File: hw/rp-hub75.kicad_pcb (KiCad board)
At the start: 2 copper layers, 45 x 45 mm, 38 parts, among them J1 Display Connector, J2 USB_C_Receptacle_USB2.0_16P, J3 Screw_Terminal_01x02, J4 Conn_01x04, J5 USB_A, J6 Conn_01x10, U1 AMS1117-3.3, U2 RP2350_60QFN, U3 W25Q128JVS, Y1 TXM12M0004322CBCDO00T

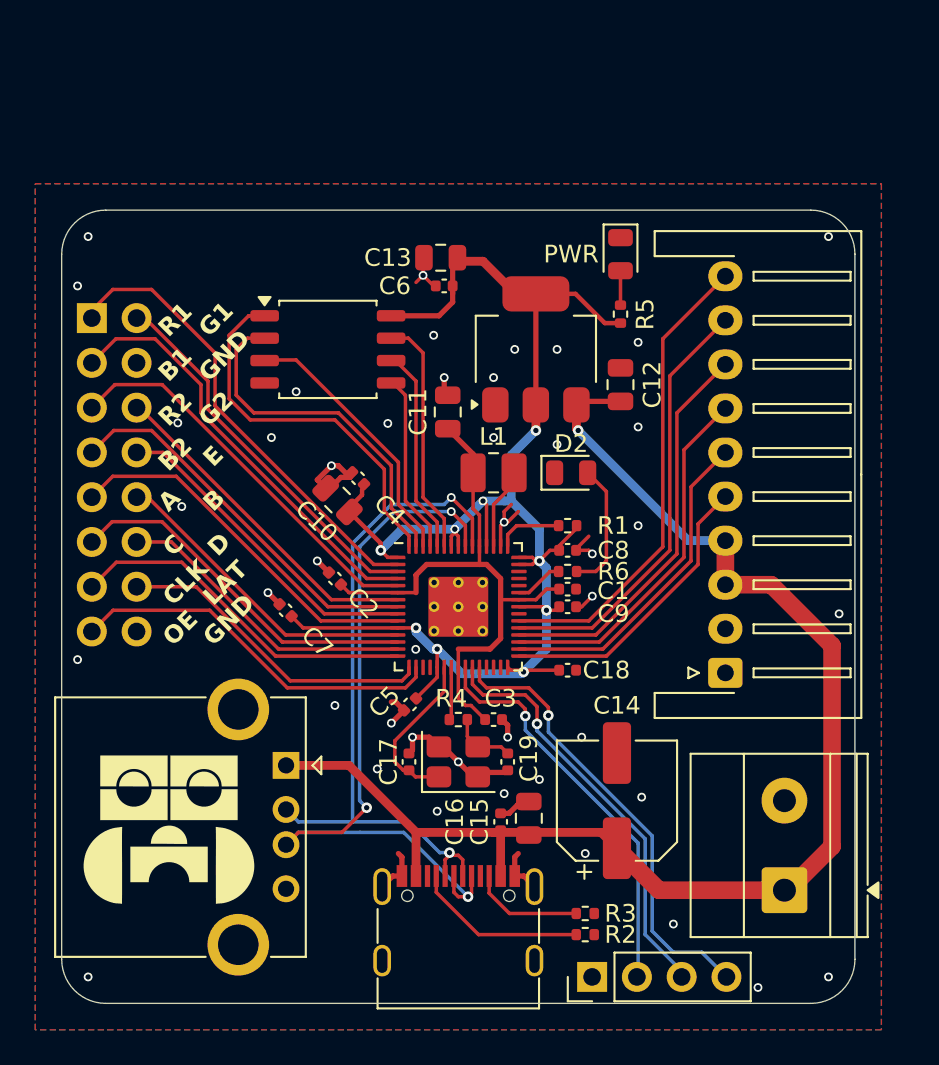
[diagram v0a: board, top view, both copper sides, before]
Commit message: hw: edit DBG connector, new capacitor
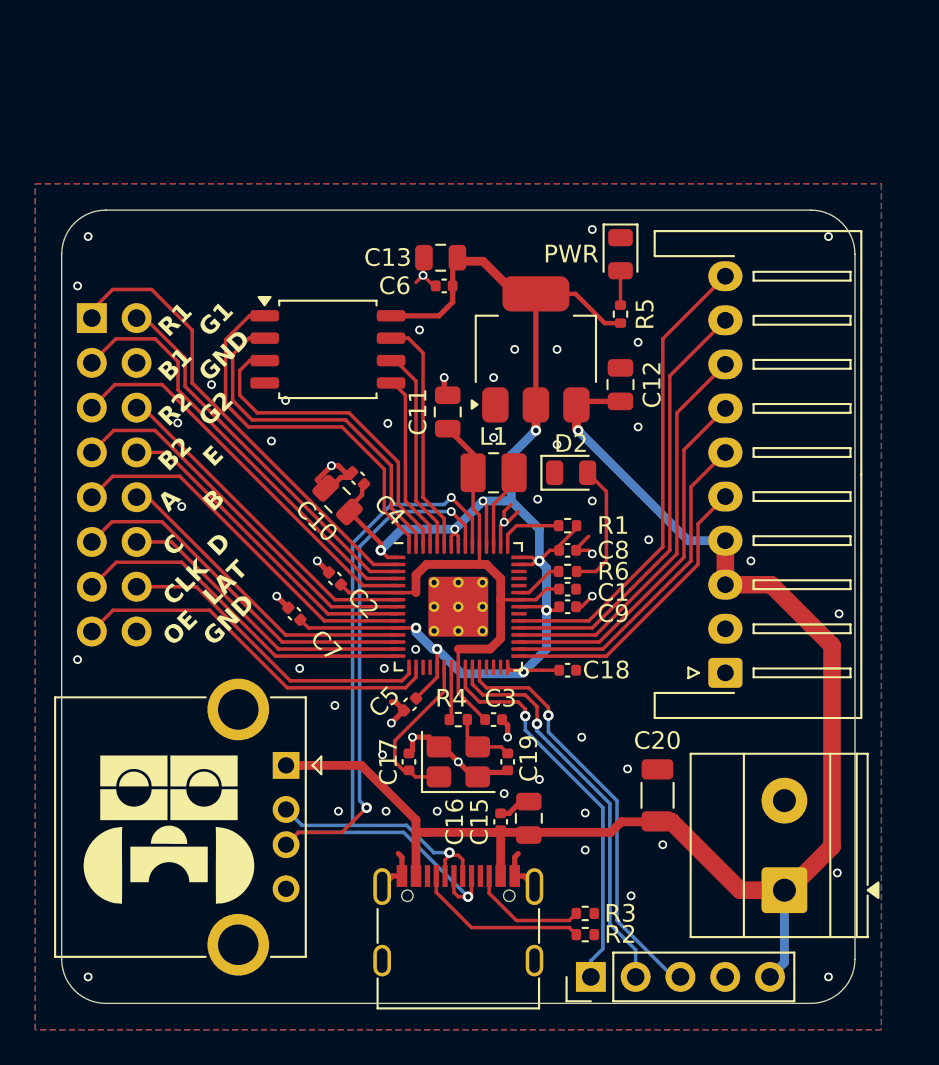
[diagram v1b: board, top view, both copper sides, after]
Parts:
- removed C14: 470u, Capacitor_SMD:CP_Elec_6.3x7.7
- removed J4: Conn_01x04, Connector_PinHeader_2.54mm:PinHeader_1x04_P2.54mm_Vertical
- added C20: 47u, Capacitor_SMD:C_1206_3216Metric, F.Cu at (211.3, 110.7)
- added J7: Conn_01x05, Connector_PinHeader_2.54mm:PinHeader_1x05_P2.54mm_Vertical, F.Cu at (207.5, 121.0)
- moved C7 0.54 mm to (190.7, 100.4)
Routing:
- net +5V: track 77.2 -> 83.4 mm
- net /QSPI_SD2: track 15.3 -> 19.0 mm
- net Net-(J7-Pin_3): track 25.7 -> 24.3 mm
- net Net-(J7-Pin_2): track 23.9 -> 22.8 mm
- net +3V3: track 87.4 -> 86.9 mm
- net Net-(J7-Pin_1): track 22.9 -> 22.4 mm
- net GND: vias 44 -> 55
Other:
- board text added: "10/2025"
- board text added: "V1.1"
- board text removed: "9/2025"
- board text removed: "V1"

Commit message: V1.2
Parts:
- added J4: Conn_01x02, Connector_PinHeader_2.54mm:PinHeader_1x02_P2.54mm_Vertical, F.Cu at (180.3, 79.4)
- added REF**: MountingHole_3.2mm_M3, MountingHole:MountingHole_3.2mm_M3, F.Cu at (181.0, 74.0)
- added REF**: MountingHole_3.2mm_M3, MountingHole:MountingHole_3.2mm_M3, F.Cu at (219.0, 106.5)
- R5, R6: value 220 -> 1k
- U3: value W25Q128JVS -> ZD25WQ80CTIGT; footprint Package_SO:SOIC-8_5.3x5.3mm_P1.27mm -> Package_SO:SOIC-8_3.9x4.9mm_P1.27mm
- moved J6 26.9 mm to (210.2, 77.3), turned to 180 degrees
- moved R3 14.2 mm to (193.1, 118.7), turned to 180 degrees
- moved R2 14.1 mm to (193.1, 117.5), turned to 180 degrees
- moved D2 13.7 mm to (209.3, 105.8)
- moved C12 8.44 mm to (211.0, 95.7), turned to -90 degrees
- moved C13 7.70 mm to (203.7, 86.3), turned to -90 degrees
- moved U1 5.46 mm to (208.5, 89.0)
- moved C6 4.82 mm to (202.0, 85.7), turned to -90 degrees
- moved D1 4.08 mm to (206.8, 83.3), turned to 0 degrees
- moved J3 3.27 mm to (219.9, 119.0)
- moved C11 2.58 mm to (201.9, 89.6), turned to 0 degrees
- moved U3 2.47 mm to (195.0, 86.0)
- moved J7 2.14 mm to (209.6, 120.5), turned to 180 degrees
- moved C20 1.68 mm to (212.9, 110.2), turned to -90 degrees
- moved J1 1.10 mm to (180.3, 83.6)
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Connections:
- J3 pad 1: +5V -> GND
- J3 pad 2: GND -> +5V
- J7 pad 1: Net-(J7-Pin_1) -> GND
- J7 pad 2: Net-(J7-Pin_2) -> +5V
- J7 pad 4: GND -> Net-(J7-Pin_4)
- J7 pad 5: +5V -> Net-(J7-Pin_5)
- U2 pad 24: Net-(J7-Pin_1) -> Net-(J7-Pin_3)
- U2 pad 25: Net-(J7-Pin_2) -> Net-(J7-Pin_4)
- U2 pad 26: Net-(J7-Pin_3) -> Net-(J7-Pin_5)
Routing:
- net Net-(J7-Pin_2): track 22.8 -> 0.00 mm, vias 1 -> 0
- net Net-(J7-Pin_1): track 22.4 -> 0.00 mm, vias 1 -> 0
- net SPI_MISO: track 16.8 -> 37.2 mm, vias 0 -> 1
- net GND: track 34.9 -> 16.2 mm, vias 55 -> 52
- net SPI_MOSI: track 18.8 -> 37.1 mm, vias 0 -> 1
- net SPI_CS: track 20.8 -> 37.0 mm, vias 0 -> 1
- net SPI_SCK: track 22.8 -> 38.1 mm, vias 0 -> 1
- net Net-(J7-Pin_4): track 0.00 -> 14.5 mm
- net SPI_X1: track 24.7 -> 39.2 mm, vias 0 -> 1
- net SPI_X2: track 26.7 -> 40.2 mm, vias 0 -> 1
- net Net-(J7-Pin_5): track 0.00 -> 11.8 mm
- net +5V: track 83.4 -> 94.4 mm, vias 1 -> 0
- net Net-(J7-Pin_3): track 24.3 -> 17.2 mm, vias 1 -> 0
- net /QSPI_SS: track 21.9 -> 28.4 mm
- net Net-(D2-A): track 7.38 -> 11.8 mm
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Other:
- board size 45 x 45 mm -> 45 x 52 mm
- board text added: "12/2025"
- board text added: "DBG"
- board text added: "V1.2"
- board text removed: "10/2025"
- board text removed: "V1.1"

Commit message: V1.3
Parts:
- added J8: Conn_01x04, Connector_PinHeader_2.54mm:PinHeader_1x04_P2.54mm_Vertical, F.Cu at (183.2, 104.7)
- moved D1 23.0 mm to (208.5, 106.2), turned to 90 degrees
- moved R5 22.1 mm to (206.2, 105.3), turned to 0 degrees
- moved R2 14.0 mm to (206.8, 120.4), turned to 0 degrees
- moved R3 13.7 mm to (206.8, 119.2), turned to 0 degrees
- moved J5 6.77 mm to (183.5, 109.8), turned to 0 degrees
- moved J6 2.00 mm to (210.2, 75.3)
- moved D2 1.46 mm to (210.7, 106.2), turned to 90 degrees
- moved C7 1.30 mm to (192.4, 100.5)
- moved U3 1.16 mm to (195.3, 87.1)
- moved C10 1.03 mm to (195.6, 93.1)
- moved C11 1.03 mm to (194.2, 94.1)
- moved C2 0.90 mm to (193.9, 98.4)
- moved C15 0.64 mm to (204.5, 111.6)
- moved C16 0.58 mm to (202.9, 111.9)
- renumbered C4 to C10, C10 to C11, C6 to C17, C17 to C18, C11 to C4, C18 to C6
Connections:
- J6 pad 2: GND -> +5V
- J6 pad 4: +5V -> SPI_MISO
- J6 pad 5: SPI_MISO -> SPI_MOSI
- J6 pad 6: SPI_MOSI -> SPI_CS
- J6 pad 7: SPI_CS -> SPI_SCK
- J6 pad 8: SPI_SCK -> GND
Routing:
- net +5V: track 94.4 -> 106.6 mm
- net D-: track 39.4 -> 45.7 mm
- net Net-(J2-CC1): track 7.23 -> 10.8 mm
- net Net-(J2-CC2): track 10.4 -> 6.98 mm
- net +3V3: track 84.4 -> 81.2 mm
- net SPI_X1: track 39.2 -> 41.2 mm
- net SPI_X2: track 40.2 -> 42.2 mm
- net /QSPI_SCLK: track 12.1 -> 10.5 mm
- net Net-(D2-A): track 11.8 -> 10.4 mm
- net /QSPI_SD0: track 9.01 -> 7.79 mm
- net D+: track 44.0 -> 45.2 mm
- net SPI_MOSI: track 37.1 -> 38.1 mm
- net SPI_CS: track 37.0 -> 38.0 mm
- net SPI_MISO: track 37.2 -> 38.2 mm
- net +1V1: track 32.8 -> 31.9 mm
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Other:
- board text added: "3V3 LDO"
- board text added: "BOOT"
- board text added: "D+"
- board text added: "D-"
- board text added: "Flash"
- board text added: "RP2350"
- board text added: "RP2350 HUB75E"
- board text added: "V1.3"
- board text added: "display driver"
- board text removed: "RP2350 HUB75E driver"
- board text removed: "V1.2"

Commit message: V1.4
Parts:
- removed J4: Conn_01x02, Connector_PinHeader_2.54mm:PinHeader_1x02_P2.54mm_Vertical
- added SW1: SW_Push, Button_Switch_SMD:SW_SPST_TS-1088-xR025, F.Cu at (181.6, 79.3)
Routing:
- net GND: track 16.4 -> 15.0 mm, vias 72 -> 71
- net SPI_MISO: track 38.2 -> 39.4 mm
- net SPI_X2: track 42.2 -> 41.1 mm
- net /QSPI_SS: track 28.6 -> 27.5 mm
- net +5V: track 106.6 -> 105.9 mm
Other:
- board text added: "V1.4"
- board text removed: "V1.3"

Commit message: V1.4b
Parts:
- removed C20: 47u, Capacitor_SMD:C_1206_3216Metric
- moved J6 1.00 mm to (210.2, 76.3)
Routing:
- net +5V: track 105.9 -> 103.8 mm
- net SPI_X1: track 41.2 -> 40.2 mm
- net SPI_SCK: track 37.9 -> 36.9 mm
- net SPI_MOSI: track 38.0 -> 37.0 mm
- net SPI_MISO: track 39.4 -> 38.4 mm
- net SPI_CS: track 38.0 -> 37.0 mm
- net SPI_X2: track 41.1 -> 40.1 mm
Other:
- board text added: "1/2026"
- board text removed: "12/2025"

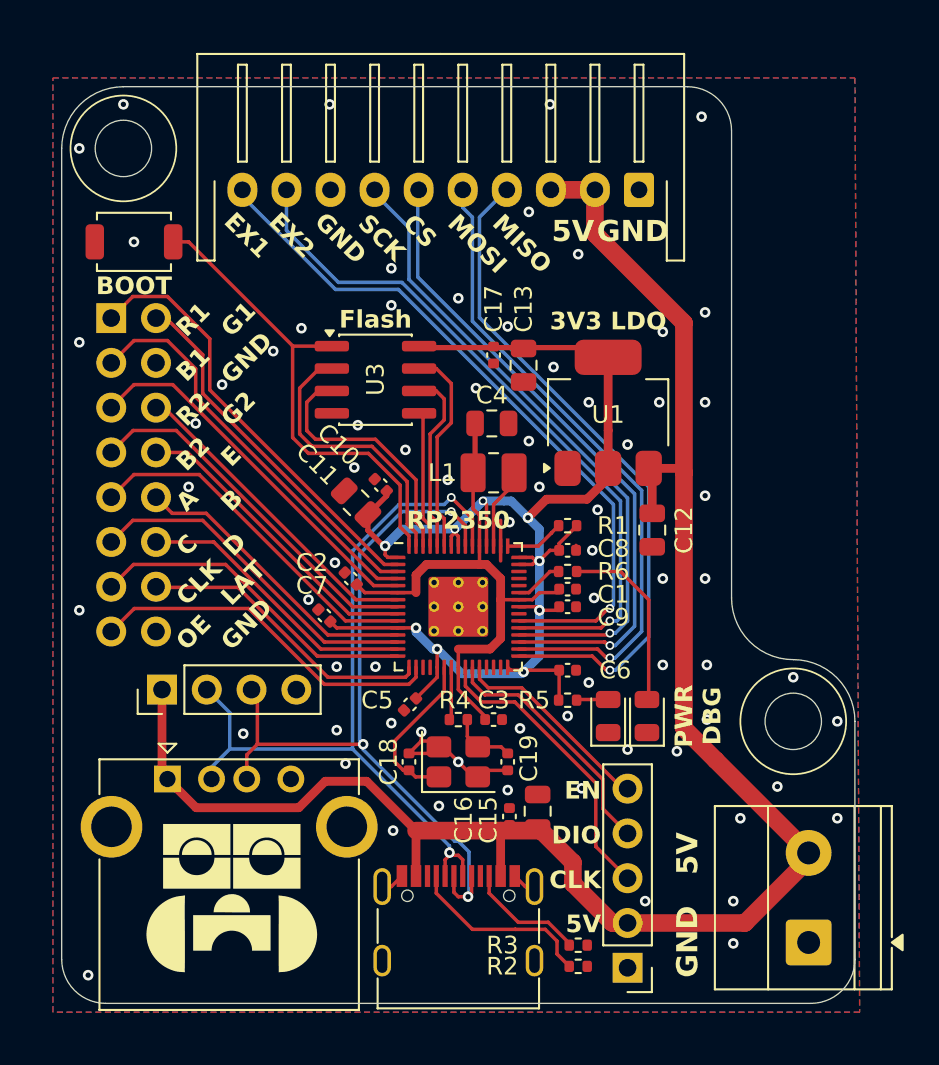
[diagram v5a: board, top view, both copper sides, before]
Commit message: v1.5 - use QSPI, better 1V1 line
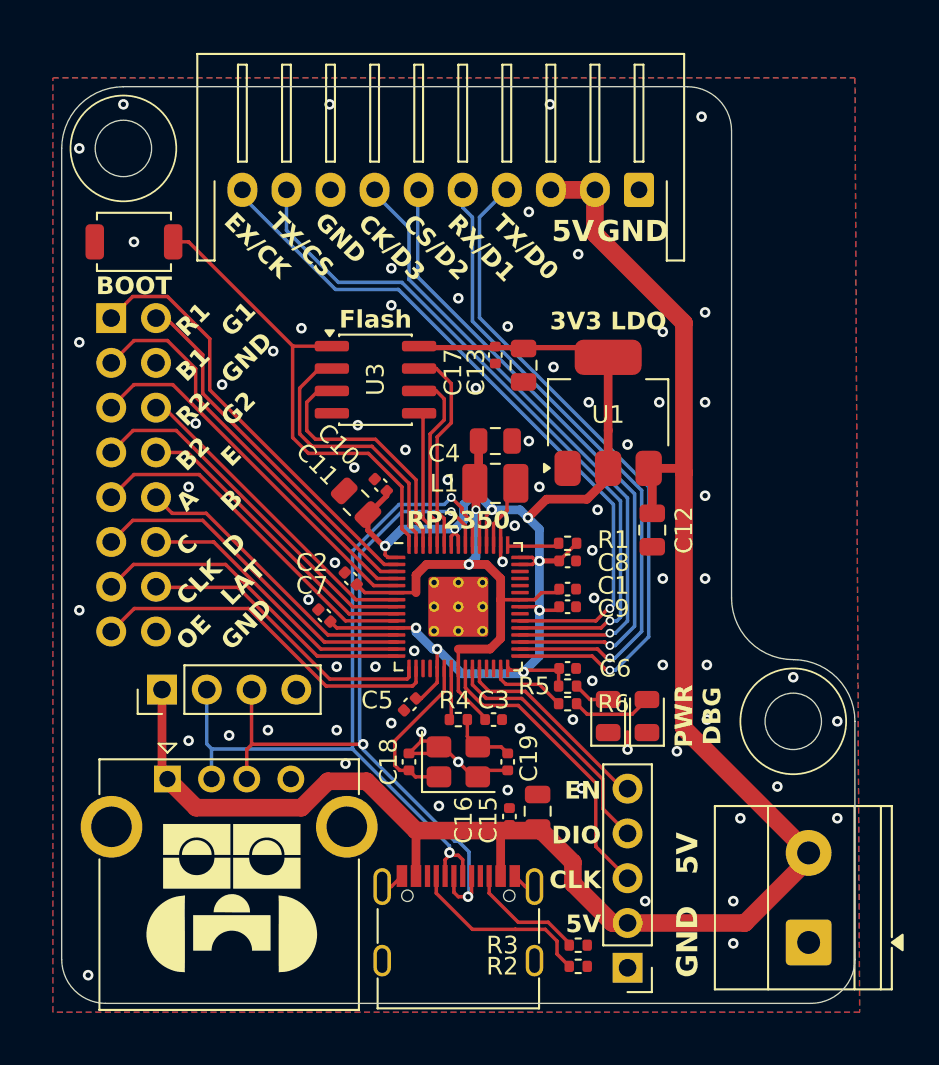
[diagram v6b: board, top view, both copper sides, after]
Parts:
- moved R6 7.50 mm to (206.2, 105.5)
- moved C4 1.02 mm to (202.1, 90.6)
- moved R1 1.00 mm to (206.2, 96.4)
- moved R5 0.80 mm to (206.2, 104.5)
- moved L1 0.61 mm to (202.1, 93.0)
- moved C8 0.60 mm to (206.2, 97.4)
- moved C17 0.10 mm to (202.1, 85.7)
- moved C6 0.10 mm to (206.2, 103.5)
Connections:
- net SPI_CS renamed SPI_CS/D2
- net SPI_MISO renamed SPI_TX/D0
- net SPI_MOSI renamed SPI_RX/D1
- net SPI_SCK renamed SPI_CK/D3
- net SPI_X1 renamed SPI_TX/CS
- net SPI_X2 renamed SPI_EX/CK
- U2 pad 29: unconnected-(U2-GPIO18-Pad29) -> STATUS
- U2 pad 40: STATUS -> unconnected-(U2-GPIO26_ADC0-Pad40)
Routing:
- net Net-(D2-A): track 10.4 -> 4.59 mm
- net STATUS: track 2.75 -> 4.53 mm
- net +1V1: track 31.9 -> 33.0 mm, vias 0 -> 2
- net +3V3: track 81.2 -> 80.3 mm
- net GND: track 15.0 -> 15.1 mm, vias 71 -> 74
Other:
- board text added: "2/2026"
- board text added: "CK/D3"
- board text added: "CS/D2"
- board text added: "EX/CK"
- board text added: "RX/D1"
- board text added: "TX/CS"
- board text added: "TX/D0"
- board text added: "V1.5"
- board text removed: "1/2026"
- board text removed: "CS"
- board text removed: "EX1"
- board text removed: "EX2"
- board text removed: "MISO"
- board text removed: "MOSI"
- board text removed: "SCK"
- board text removed: "V1.4"

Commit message: v1.6
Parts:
- removed J8: Conn_01x04, Connector_PinHeader_2.54mm:PinHeader_1x04_P2.54mm_Vertical
- added J4: Conn_01x03, Connector_PinHeader_2.54mm:PinHeader_1x03_P2.54mm_Vertical, F.Cu at (183.5, 106.0)
- moved C13 10.7 mm to (208.8, 95.7)
- moved C17 1.70 mm to (203.8, 85.8)
- moved C5 1.01 mm to (196.6, 106.3)
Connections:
- U2 pad 18: unconnected-(U2-GPIO14-Pad18) -> SDA
- U2 pad 19: unconnected-(U2-GPIO15-Pad19) -> SCL
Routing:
- net SCL: track 0.00 -> 15.0 mm
- net SDA: track 0.00 -> 11.0 mm
- net +5V: track 103.8 -> 98.7 mm
- net D-: track 45.9 -> 42.1 mm
- net D+: track 45.2 -> 41.7 mm
- net +3V3: track 80.3 -> 82.9 mm
- net GND: vias 74 -> 77
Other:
- board text added: "&"
- board text added: "14"
- board text added: "15"
- board text added: "4/2026"
- board text added: "C2Coder"
- board text added: "CK"
- board text added: "CS"
- board text added: "D0"
- board text added: "D1"
- board text added: "D2"
- board text added: "D3"
- board text added: "G"
- board text added: "RP2350 HUB75"
- board text added: "V1.6"
- board text added: "https://hub75.robotikabrno.cz"
- board text removed: "2/2026"
- board text removed: "3V3 LDO"
- board text removed: "CK/D3"
- board text removed: "CS/D2"
- board text removed: "D+"
- board text removed: "D-"
- board text removed: "EX/CK"
- board text removed: "Flash"
- board text removed: "RP2350"
- board text removed: "RP2350 HUB75E"
- board text removed: "RX/D1"
- board text removed: "TX/CS"
- board text removed: "TX/D0"
- board text removed: "V1.5"
- board text removed: "github.com/RoboticsBrno/RP-HUB75"

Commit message: v1.7
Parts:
- removed J6: Conn_01x10, Connector_JST:JST_XH_S10B-XH-A-1_1x10_P2.50mm_Horizontal
- removed the REF** at (181.0, 74.0)
- added J8: ZX-XH2.54-10PWT, Library:JST-XH-SMD-10Pin, F.Cu at (198.5, 76.0)
- moved SW1 3.85 mm to (181.0, 75.5), turned to -90 degrees
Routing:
- net /QSPI_SS: track 27.5 -> 31.5 mm
- net +5V: track 98.7 -> 96.4 mm
- net SPI_EX/CK: track 40.1 -> 41.7 mm, vias 1 -> 2
- net SPI_TX/CS: track 40.2 -> 41.4 mm, vias 1 -> 2
- net SPI_RX/D1: track 37.0 -> 37.8 mm, vias 1 -> 2
- net SPI_CK/D3: track 36.9 -> 37.6 mm, vias 1 -> 2
- net SPI_CS/D2: track 37.0 -> 37.7 mm, vias 1 -> 2
- net SPI_TX/D0: track 38.4 -> 39.1 mm, vias 1 -> 2
- net GND: vias 77 -> 84
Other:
- board text added: "5/2026"
- board text added: "D+"
- board text added: "D-"
- board text added: "Uhhh, hey there, where is the connector?"
- board text added: "V1.7"
- board text added: "hub75.robotikabrno.cz"
- board text removed: "4/2026"
- board text removed: "V1.6"
- board text removed: "https://hub75.robotikabrno.cz"
